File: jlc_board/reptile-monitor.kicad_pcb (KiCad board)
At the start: 4 copper layers, 38.1 x 38 mm, 39 parts, among them J1 1-WIRE, J2 UART, J3 Conn_01x04, J6 I/O, J8 I2C, SW1 RESET, SW2 BOOT, U1 AP2112M-3.3

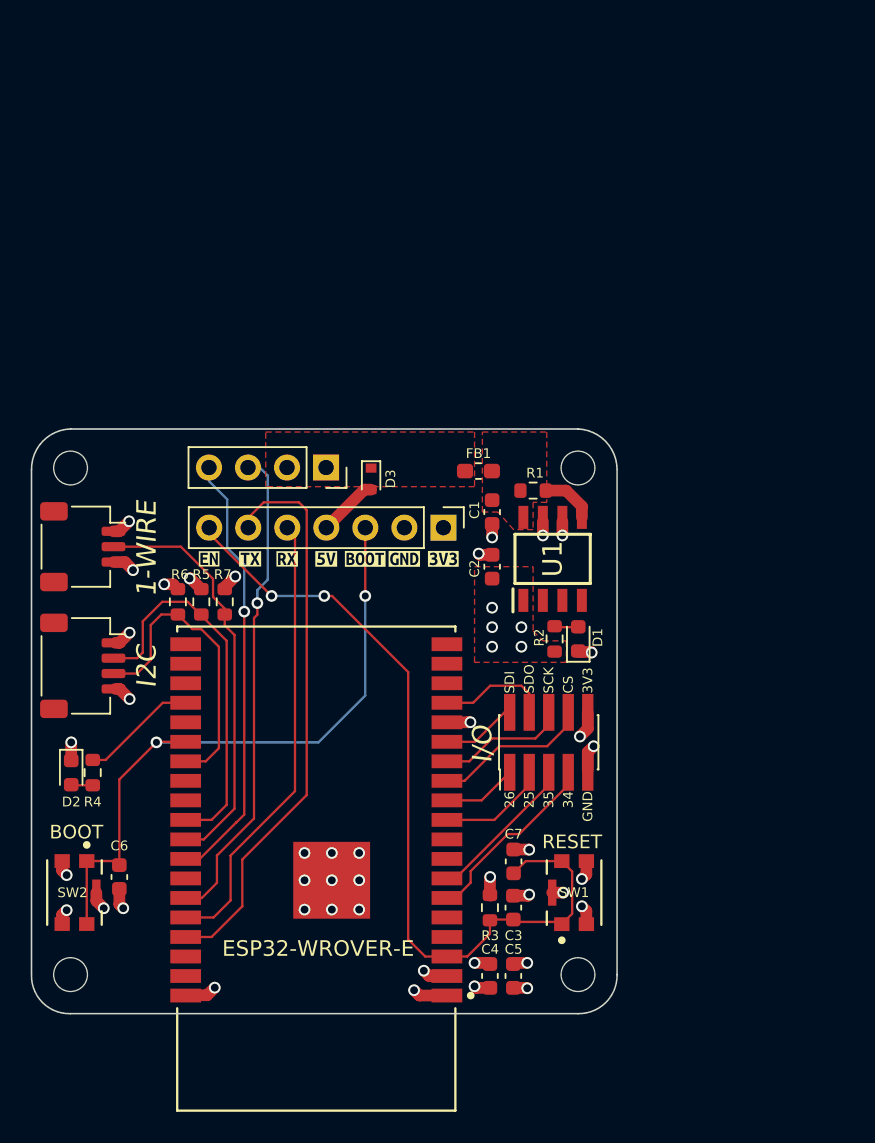
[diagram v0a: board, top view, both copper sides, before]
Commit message: Rev 3 - separate power board
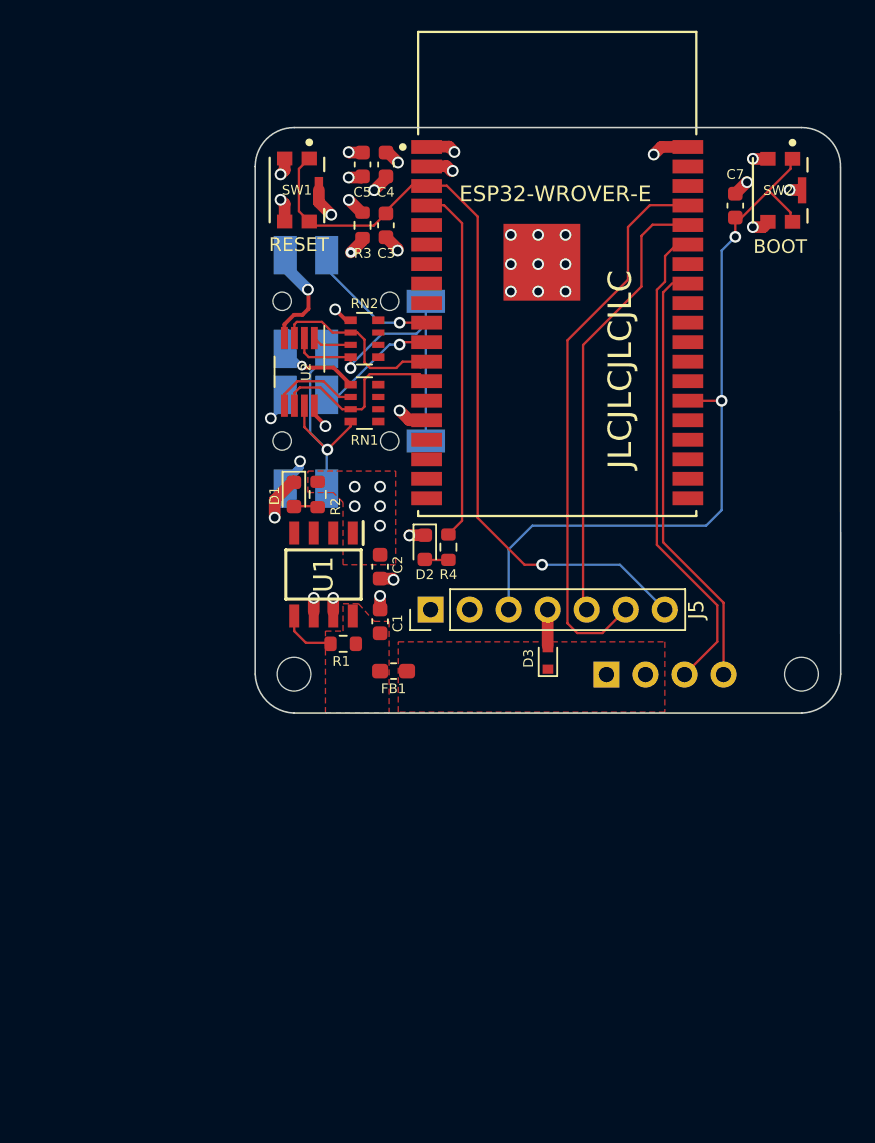
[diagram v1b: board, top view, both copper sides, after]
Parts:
- removed C6: 100n, Capacitor_SMD:C_0603_1608Metric
- removed J6: I/O, Connector_PinHeader_1.27mm:PinHeader_2x05_P1.27mm_Vertical_SMD
- removed J8: I2C, Connector_JST:JST_SH_SM04B-SRSS-TB_1x04-1MP_P1.00mm_Horizontal
- removed R5, R6, R7: 10k, Resistor_SMD:R_0603_1608Metric
- removed the REF1 at (104.1, 132.8)
- removed the REF1 at (137.2, 132.8)
- removed svg2mod (x7): G***, svg2mod
- added J5: UART, Connector_PinHeader_2.54mm:PinHeader_1x07_P2.54mm_Vertical, F.Cu at (127.6, 109.1)
- added RN1: 10k, Resistor_SMD:R_Array_Convex_4x0603, F.Cu at (123.3, 95.7)
- added RN2: 10k, Resistor_SMD:R_Array_Convex_4x0603, F.Cu at (123.3, 91.5)
- added U2: TCA4307DGKR, Package_SO:VSSOP-8_3.0x3.0mm_P0.65mm, F.Cu at (119.0, 93.6)
- J1: value 1-WIRE -> AudioJack4_SwitchR1; footprint Connector_JST:JST_SH_SM03B-SRSS-TB_1x03-1MP_P1.00mm_Horizontal -> reptile-monitor:Korean Hroparts Elec PJ-227-5A; moved to B.Cu
- J2: value UART -> AudioJack4_SwitchR1; footprint Connector_PinHeader_2.54mm:PinHeader_1x07_P2.54mm_Vertical -> reptile-monitor:Korean Hroparts Elec PJ-227-5A; moved to B.Cu
- J3: value Conn_01x04 -> PWR CONN; moved to B.Cu
- moved SW2 64.8 mm to (150.3, 81.8)
- moved C5 53.7 mm to (123.1, 80.1), turned to 90 degrees
- moved C4 53.2 mm to (124.7, 80.1), turned to 90 degrees
- moved REF1 49.4 mm to (151.7, 113.3), turned to 180 degrees
- moved SW1 49.1 mm to (118.9, 81.8), turned to -90 degrees
- moved C3 45.2 mm to (124.7, 84.1)
- moved R3 45.2 mm to (123.1, 84.1)
- moved C7 45.0 mm to (147.4, 82.8), turned to -90 degrees
- moved MD1 41.8 mm to (135.8, 87.2), turned to 0 degrees
- moved WAFFLE 32.3 mm to (140.4, 92.7), turned to 180 degrees
- moved R4 27.4 mm to (128.7, 105.0)
- moved D2 27.3 mm to (127.2, 105.0)
- moved REF2 22.8 mm to (118.7, 113.3), turned to 180 degrees
- moved J3 22.7 mm to (139.0, 113.3)
- moved D1 20.8 mm to (118.7, 101.6), turned to -90 degrees
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- renumbered REF1 to REF2
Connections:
- C3 pad 1: EN -> GND
- C3 pad 2: GND -> EN
- C7 pad 1: EN -> GND
- C7 pad 2: GND -> BOOT
- J1 pad 1: GND -> +3V3
- J1 pad 2: 1-WIRE -> SCL_BUFFERED
- J1 pad 3: +3V3 -> SDA_BUFFERED
- J2 pad 2: GND -> SCL_BUFFERED
- J2 pad 3: BOOT -> SDA_BUFFERED
- J2 pad 4: Net-(D3-Pad2) -> GND
- J2 pad 5: RXD0 -> IO26
- J3 pad 3: L2 -> L1
- J3 pad 4: L1 -> L2
- MD1 pad 12: CS0 -> SCL
- MD1 pad 13: SCK -> SDA
- MD1 pad 14: SDI -> (no net)
- MD1 pad 16: SDO -> (no net)
- MD1 pad 23: /LED -> (no net)
- MD1 pad 26: SCL -> (no net)
- MD1 pad 29: SDA -> (no net)
- MD1 pad 30: 1-WIRE -> (no net)
- MD1 pad 31: L1 -> L2
- MD1 pad 33: L2 -> L1
- MD1 pad 4: (no net) -> /LED
- MD1 pad 6: IO34 -> (no net)
- MD1 pad 7: IO35 -> (no net)
- R3 pad 1: EN -> GND
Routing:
- net 1-WIRE: track 26.9 -> 0.00 mm
- net SCL_BUFFERED: track 0.00 -> 20.1 mm, vias 0 -> 1
- net SDA_BUFFERED: track 0.00 -> 15.9 mm, vias 0 -> 1
- net /LED: track 7.59 -> 23.5 mm
- net SDA: track 24.9 -> 12.3 mm
- net IO34: track 10.8 -> 0.00 mm
- net CS0: track 9.40 -> 0.00 mm
- net IO35: track 8.59 -> 0.00 mm
- net GND: track 27.9 -> 35.9 mm
- net SCK: track 7.60 -> 0.00 mm
- net SCL: track 19.8 -> 12.4 mm
- net SDO: track 7.25 -> 0.00 mm
- net Net-(RN1-Pad2): track 0.00 -> 5.83 mm
- net BOOT: track 43.3 -> 49.0 mm
- net L1: track 26.7 -> 31.8 mm, vias 1 -> 0
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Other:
- board size 38.1 x 38 mm -> 38.1 x 38.1 mm
- board text added: "Mike Pleimann"
- board text removed: "25"
- board text removed: "26"
- board text removed: "34"
- board text removed: "35"
- board text removed: "3V3"
- board text removed: "CS"
- board text removed: "GND"
- board text removed: "SCK"
- board text removed: "SDI"
- board text removed: "SDO"

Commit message: consolidate kicad libraries
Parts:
- added J4: UART, reptile-monitor:PinHeader_1x07_P2.54mm_Vertical, F.Cu at (127.6, 109.1)
- added J6: I2C, reptile-monitor:JST_SH_SM04B-SRSS-TB_1x04-1MP_P1.00mm_Horizontal, F.Cu at (151.5, 90.7)
- added R5: 10k, reptile-monitor:R_0603_1608Metric, F.Cu at (146.6, 90.2)
- added R6: 10k, reptile-monitor:R_0603_1608Metric, F.Cu at (146.6, 93.1)
- C1, C2, C3, C4, C5, C7: footprint Capacitor_SMD:C_0603_1608Metric -> reptile-monitor:C_0603_1608Metric
- D1: value RED -> PWR; footprint LED_SMD:LED_0603_1608Metric -> reptile-monitor:LED_0603_1608Metric
- D2: value BLUE -> IO18; footprint LED_SMD:LED_0603_1608Metric -> reptile-monitor:LED_0603_1608Metric
- D3: footprint Diode_SMD:D_SOD-523 -> reptile-monitor:D_SOD-523
- FB1: footprint Inductor_SMD:L_0603_1608Metric_Pad1.05x0.95mm_HandSolder -> reptile-monitor:L_0603_1608Metric_Pad1.05x0.95mm_HandSolder
- J3: footprint Connector_PinSocket_2.54mm:PinSocket_1x04_P2.54mm_Vertical -> reptile-monitor:PinSocket_1x04_P2.54mm_Vertical
- J5: value UART -> I2C; footprint Connector_PinHeader_2.54mm:PinHeader_1x07_P2.54mm_Vertical -> reptile-monitor:JST_SH_SM04B-SRSS-TB_1x04-1MP_P1.00mm_Horizontal
- R1, R2, R3, R4: footprint Resistor_SMD:R_0603_1608Metric -> reptile-monitor:R_0603_1608Metric
- RN1, RN2: footprint Resistor_SMD:R_Array_Convex_4x0603 -> reptile-monitor:R_Array_Convex_4x0603
- U1: footprint SamacSys_Parts:SOIC127P600X170-8N -> reptile-monitor:SOIC127P600X170-8N
- U2: footprint Package_SO:VSSOP-8_3.0x3.0mm_P0.65mm -> reptile-monitor:VSSOP-8_3.0x3.0mm_P0.65mm
- WAFFLE: footprint LOGO -> reptile-monitor:LOGO
- moved J5 26.1 mm to (151.5, 98.6)
- moved D2 23.5 mm to (150.7, 105.8)
- moved R4 20.4 mm to (149.2, 105.8)
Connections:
- J5 pad 1: +3V3 -> SCL0
- J5 pad 2: GND -> SDA0
- J5 pad 3: BOOT -> +3V3
- J5 pad 4: Net-(D3-Pad2) -> GND
- MD1 pad 12: SCL -> (no net)
- MD1 pad 13: SDA -> (no net)
- MD1 pad 26: (no net) -> SCL0
- MD1 pad 29: (no net) -> SDA0
- MD1 pad 30: (no net) -> /LED
- MD1 pad 4: /LED -> (no net)
- MD1 pad 8: (no net) -> SDA1
- MD1 pad 9: (no net) -> SCL1
- RN1 pad 3: SDA -> SDA1
- RN2 pad 2: SCL -> SCL1
- U2 pad 3: SCL -> SCL1
- U2 pad 6: SDA -> SDA1
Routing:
- net SDA1: track 0.00 -> 21.3 mm
- net SCL0: track 0.00 -> 16.5 mm
- net SDA0: track 0.00 -> 16.4 mm
- net SCL1: track 0.00 -> 14.9 mm
- net SCL: track 12.4 -> 0.00 mm
- net SDA: track 12.3 -> 0.00 mm
- net BOOT: track 49.0 -> 42.4 mm
- net +3V3: track 15.8 -> 22.1 mm, vias 13 -> 17
- net GND: track 35.9 -> 39.4 mm, vias 32 -> 33
- net L1: track 31.8 -> 30.4 mm
- net EN: track 51.8 -> 52.5 mm
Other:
- outline, holes or cut-outs redrawn
- board text added: "3V3"
- board text added: "5V"
- board text added: "BOOT"
- board text added: "EN"
- board text added: "GND"
- board text added: "L1 IO21"
- board text added: "L2 IO19"
- board text added: "RX"
- board text added: "TX"

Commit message: rev4
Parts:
- C1, C2, C3, C4, C5, C7: footprint reptile-monitor:C_0603_1608Metric -> Capacitor_SMD:C_0603_1608Metric
- D1: value PWR -> RED; footprint reptile-monitor:LED_0603_1608Metric -> LED_SMD:LED_0603_1608Metric
- D2: value IO18 -> BLU; footprint reptile-monitor:LED_0603_1608Metric -> LED_SMD:LED_0603_1608Metric
- D3: footprint reptile-monitor:D_SOD-523 -> Diode_SMD:D_SOD-523
- FB1: footprint reptile-monitor:L_0603_1608Metric_Pad1.05x0.95mm_HandSolder -> Inductor_SMD:L_0603_1608Metric_Pad1.05x0.95mm_HandSolder
- J3: footprint reptile-monitor:PinSocket_1x04_P2.54mm_Vertical -> Connector_PinSocket_2.54mm:PinSocket_1x04_P2.54mm_Vertical
- J4: footprint reptile-monitor:PinHeader_1x07_P2.54mm_Vertical -> Connector_PinHeader_2.54mm:PinHeader_1x07_P2.54mm_Vertical
- J5, J6: footprint reptile-monitor:JST_SH_SM04B-SRSS-TB_1x04-1MP_P1.00mm_Horizontal -> Connector_JST:JST_SH_SM04B-SRSS-TB_1x04-1MP_P1.00mm_Horizontal
- R1, R2, R3, R4, R5, R6: footprint reptile-monitor:R_0603_1608Metric -> Resistor_SMD:R_0603_1608Metric
- RN1, RN2: footprint reptile-monitor:R_Array_Convex_4x0603 -> Resistor_SMD:R_Array_Convex_4x0603
- U2: footprint reptile-monitor:VSSOP-8_3.0x3.0mm_P0.65mm -> Package_SO:VSSOP-8_3.0x3.0mm_P0.65mm
- moved D1 32.6 mm to (151.1, 105.3)
- moved R2 32.6 mm to (152.6, 105.3)
- moved J1 9.78 mm to (116.1, 98.8)
- moved RN1 9.40 mm to (122.6, 105.0)
- moved RN2 9.40 mm to (122.6, 100.8)
- moved U2 9.26 mm to (118.6, 102.9)
- moved J2 8.95 mm to (116.1, 107.1)
- moved R1 8.94 mm to (130.8, 112.4), turned to 90 degrees
- moved FB1 8.44 mm to (133.6, 112.3), turned to 90 degrees
- moved C1 7.90 mm to (132.2, 110.5)
- moved U1 7.72 mm to (126.1, 112.3), turned to 0 degrees
- moved C2 6.36 mm to (121.5, 112.0)
- moved J4 2.96 mm to (129.6, 106.9)
- moved WAFFLE 2.62 mm to (137.9, 92.2)
- moved D3 1.62 mm to (136.3, 111.1)
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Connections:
- RN1 pad 3: SDA1 -> SDA_BUFFERED
- RN1 pad 4: SDA_BUFFERED -> SDA1
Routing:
- net SCL1: track 14.9 -> 28.9 mm
- net SDA1: track 21.3 -> 30.1 mm
- net IO26: track 7.92 -> 14.9 mm
- net TXD0: track 36.5 -> 31.7 mm
- net RXD0: track 29.2 -> 25.1 mm
- net +3V3: track 22.1 -> 19.2 mm, vias 17 -> 22
- net /LED: track 23.2 -> 20.4 mm
- net SCL_BUFFERED: track 20.1 -> 17.3 mm
- net SDA_BUFFERED: track 16.0 -> 14.0 mm
- net Net-(D3-Pad2): track 2.03 -> 3.86 mm
- net SCL0: track 16.5 -> 15.0 mm
- net /PWR_EN: track 3.39 -> 2.06 mm
- net BOOT: track 42.4 -> 41.2 mm
- net IO25: track 7.94 -> 9.11 mm
- net EN: track 52.5 -> 51.6 mm
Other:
- rule pad_to_mask_clearance: 0.0508 -> 0
- board text added: "Rev. 4 Aug 2021"
- board text removed: "Rev. 3 July 2021"

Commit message: move quiic connector to same side as TRRS sensor connectors so that all connectors are on the same side
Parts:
- removed FB1: 360 m, Inductor_SMD:L_0603_1608Metric_Pad1.05x0.95mm_HandSolder
- removed J6: I2C, Connector_JST:JST_SH_SM04B-SRSS-TB_1x04-1MP_P1.00mm_Horizontal
- removed R5, R6: 10k, Resistor_SMD:R_0603_1608Metric
- added C6: 100n, reptile-monitor:C_0603_1608Metric, F.Cu at (120.1, 107.3)
- added C8: 100n, reptile-monitor:C_0603_1608Metric, F.Cu at (118.2, 96.5)
- added L1: 360 m, reptile-monitor:L_0603_1608Metric, F.Cu at (133.4, 112.3)
- C1, C2, C3, C4, C5, C7: footprint Capacitor_SMD:C_0603_1608Metric -> reptile-monitor:C_0603_1608Metric
- D1: value RED -> PWR; footprint LED_SMD:LED_0603_1608Metric -> reptile-monitor:LED_0603_1608Metric
- D2: value BLU -> 18; footprint LED_SMD:LED_0603_1608Metric -> reptile-monitor:LED_0603_1608Metric
- D3: footprint Diode_SMD:D_SOD-523 -> reptile-monitor:D_SOD-523
- J3: footprint Connector_PinSocket_2.54mm:PinSocket_1x04_P2.54mm_Vertical -> reptile-monitor:PinSocket_1x04_P2.54mm_Vertical
- J4: footprint Connector_PinHeader_2.54mm:PinHeader_1x07_P2.54mm_Vertical -> reptile-monitor:PinHeader_1x07_P2.54mm_Vertical
- J5: footprint Connector_JST:JST_SH_SM04B-SRSS-TB_1x04-1MP_P1.00mm_Horizontal -> reptile-monitor:JST_SH_SM04B-SRSS-TB_1x04-1MP_P1.00mm_Horizontal
- R1, R2, R3, R4: footprint Resistor_SMD:R_0603_1608Metric -> reptile-monitor:R_0603_1608Metric
- RN1, RN2: footprint Resistor_SMD:R_Array_Convex_4x0603 -> reptile-monitor:R_Array_Convex_4x0603
- U2: footprint Package_SO:VSSOP-8_3.0x3.0mm_P0.65mm -> reptile-monitor:VSSOP-8_3.0x3.0mm_P0.65mm
- moved J5 33.6 mm to (118.9, 90.0), turned to -90 degrees
- moved RN1 3.98 mm to (123.8, 101.2), turned to 90 degrees
- moved RN2 3.98 mm to (123.8, 104.6), turned to -90 degrees
- moved R4 1.65 mm to (147.8, 106.9)
- moved D1 1.65 mm to (151.1, 106.9)
- moved D2 1.65 mm to (149.3, 106.9)
- moved R2 1.65 mm to (152.6, 106.9)
- moved U2 0.40 mm to (118.9, 103.0), turned to 90 degrees
- moved C1 0.38 mm to (132.2, 110.1)
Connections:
- net Net-(D3-Pad2) renamed /5V_IN
- J1 pad 5: IO25 -> IO35
- J2 pad 2: SCL_BUFFERED -> IO27
- J2 pad 3: SDA_BUFFERED -> IO26
- J2 pad 5: IO26 -> IO25
- J5 pad 1: SCL0 -> SCL_BUFFERED
- J5 pad 2: SDA0 -> SDA_BUFFERED
- MD1 pad 12: (no net) -> IO27
- MD1 pad 26: SCL0 -> (no net)
- MD1 pad 29: SDA0 -> (no net)
- MD1 pad 7: (no net) -> IO35
- MD1 pad 8: SDA1 -> SCL0
- MD1 pad 9: SCL1 -> SDA0
- RN1 pad 2: Net-(RN1-Pad2) -> SDA_BUFFERED
- RN1 pad 3: SDA_BUFFERED -> SDA0
- RN1 pad 4: SDA1 -> /U2_RDY
- RN2 pad 2: SCL1 -> /U2_EN
- RN2 pad 3: Net-(RN2-Pad3) -> SCL0
- RN2 pad 5: (no net) -> IO26
- U2 pad 1: Net-(RN2-Pad3) -> /U2_EN
- U2 pad 3: SCL1 -> SCL0
- U2 pad 5: Net-(RN1-Pad2) -> /U2_RDY
- U2 pad 6: SDA1 -> SDA0
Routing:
- net SDA1: track 30.1 -> 0.00 mm
- net SCL1: track 28.9 -> 0.00 mm
- net IO27: track 0.00 -> 16.1 mm, vias 0 -> 1
- net SCL0: track 15.0 -> 28.7 mm
- net IO35: track 0.00 -> 13.4 mm, vias 0 -> 1
- net /U2_EN: track 0.00 -> 11.2 mm
- net SCL_BUFFERED: track 17.3 -> 28.0 mm, vias 1 -> 2
- net IO26: track 14.9 -> 25.2 mm, vias 1 -> 2
- net SDA0: track 16.8 -> 26.6 mm
- net BOOT: track 41.2 -> 49.4 mm, vias 2 -> 1
- net IO25: track 9.11 -> 17.3 mm
- net SDA_BUFFERED: track 14.0 -> 21.2 mm
- net Net-(RN1-Pad2): track 6.19 -> 0.00 mm
- net /U2_RDY: track 0.00 -> 5.60 mm
- net GND: track 39.5 -> 36.2 mm
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
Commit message: v4 reorganization complete
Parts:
- removed C7: 100n, reptile-monitor:C_0603_1608Metric
- removed REF1, REF2: MountingHole_2.2mm_M2_ISO7380, MountingHole:MountingHole_2.2mm_M2_ISO7380
- removed SW2: BOOT, reptile-monitor:CK-KMR221GLFS-MFG
- added H1: MountingHole, MountingHole:MountingHole_2.2mm_M2_ISO7380, F.Cu at (118.7, 80.3)
- added H2: MountingHole, MountingHole:MountingHole_2.2mm_M2_ISO7380, F.Cu at (151.7, 80.3)
- added J6: 18-Lead FPC 0.5 mm - Vertical, reptile-monitor:TE_1-1734742-8, F.Cu at (135.2, 110.5)
- D2: value 18 -> IO5
- D3: footprint reptile-monitor:D_SOD-523 -> reptile-monitor:D_SMA
- J3: footprint reptile-monitor:PinSocket_1x04_P2.54mm_Vertical -> reptile-monitor:PinSocket_1x04_P2.54mm_Vertical_SMD_Pin1Left
- J4: footprint reptile-monitor:PinHeader_1x07_P2.54mm_Vertical -> reptile-monitor:PinHeader_1x06_P2.54mm_Vertical
- J5: moved to B.Cu
- moved J2 43.7 mm to (154.3, 85.9), turned to 180 degrees
- moved D1 40.6 mm to (117.6, 84.1), turned to 90 degrees
- moved R2 40.5 mm to (119.2, 84.1), turned to 90 degrees
- moved J1 38.5 mm to (154.3, 94.1), turned to 180 degrees
- moved C6 37.2 mm to (150.3, 85.6), turned to 180 degrees
- moved U2 35.0 mm to (151.5, 89.9), turned to -90 degrees
- moved J5 35.0 mm to (151.5, 102.9)
- moved J3 33.2 mm to (132.5, 80.8)
- moved C8 32.1 mm to (150.3, 95.5), turned to 180 degrees
- moved R4 29.3 mm to (123.8, 90.0)
- moved D2 29.0 mm to (123.8, 93.2), turned to 90 degrees
- moved SW1 29.0 mm to (120.0, 110.7), turned to 90 degrees
- moved RN2 28.1 mm to (146.6, 88.3), turned to 90 degrees
- moved C2 28.0 mm to (120.7, 84.1), turned to -90 degrees
- moved RN1 24.8 mm to (146.6, 91.7), turned to -90 degrees
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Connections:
- net Net-(C1-Pad1) renamed /PWR_IN
- J1 pad 5: IO35 -> IO15
- J2 pad 2: IO27 -> IO23
- J2 pad 3: IO26 -> IO5
- J2 pad 5: IO25 -> IO4
- J4 pad 1: +3V3 -> GND
- J4 pad 2: GND -> BOOT
- J4 pad 3: BOOT -> /5V_IN
- J4 pad 4: /5V_IN -> RXD0
- J4 pad 5: RXD0 -> TXD0
- J4 pad 6: TXD0 -> EN
- MD1 pad 13: (no net) -> SPI_SCK
- MD1 pad 14: (no net) -> SPI_SDI
- MD1 pad 16: (no net) -> SPI_SDO
- MD1 pad 23: (no net) -> IO15
- MD1 pad 26: (no net) -> IO4
- MD1 pad 29: (no net) -> IO5
- MD1 pad 30: /LED -> L2
- MD1 pad 31: L2 -> L1
- MD1 pad 33: L1 -> SDA0
- MD1 pad 36: (no net) -> SCL0
- MD1 pad 37: (no net) -> IO23
- MD1 pad 7: IO35 -> (no net)
- MD1 pad 8: SCL0 -> (no net)
- MD1 pad 9: SDA0 -> /LED
- R3 pad 1: GND -> EN
- RN2 pad 5: IO26 -> IO5
- SW1 pad 1: EN -> GND
- SW1 pad 2: EN -> GND
- SW1 pad 3: GND -> EN
- SW1 pad 4: GND -> EN
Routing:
- net BOOT: track 49.4 -> 13.1 mm, vias 1 -> 0
- net +5V: track 0.00 -> 23.7 mm, vias 0 -> 1
- net SPI_SCK: track 0.00 -> 22.9 mm
- net /5V_IN: track 3.86 -> 25.6 mm, vias 0 -> 1
- net SPI_SDO: track 0.00 -> 19.5 mm
- net SPI_SDI: track 0.00 -> 19.1 mm
- net /LED: track 21.2 -> 2.17 mm
- net L2: track 27.8 -> 10.5 mm, vias 0 -> 1
- net L1: track 30.5 -> 14.3 mm, vias 0 -> 1
- net EN: track 51.6 -> 67.0 mm, vias 1 -> 2
- net IO5: track 0.00 -> 15.2 mm, vias 0 -> 2
- net IO35: track 13.4 -> 0.00 mm, vias 1 -> 0
- net IO4: track 0.00 -> 12.2 mm, vias 0 -> 1
- net SDA0: track 26.6 -> 15.2 mm
- net IO27: track 16.1 -> 27.2 mm, vias 1 -> 2
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- removed copper zone on F.Cu, net +5V
- removed copper zone on F.Cu, net /PWR_IN
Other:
- board text added: "L1 IO19"
- board text added: "L2 IO18"
- board text removed: "3V3"
- board text removed: "L1 IO21"
- board text removed: "L2 IO19"
